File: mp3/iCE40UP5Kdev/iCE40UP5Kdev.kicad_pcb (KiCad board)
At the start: 2 copper layers, 21.8 x 51.9 mm, 57 parts, among them J1 USB4105-GF-A, J2 Left, J3 Right, J4 Conn_02x03_Counter_Clockwise, U1 W25Q32JV, U2 MIC5365-1-2YD5, U3 MIC5318-3-3YD5, U4 ICE40UP5K-SG48ITR, X1 IQXO-791

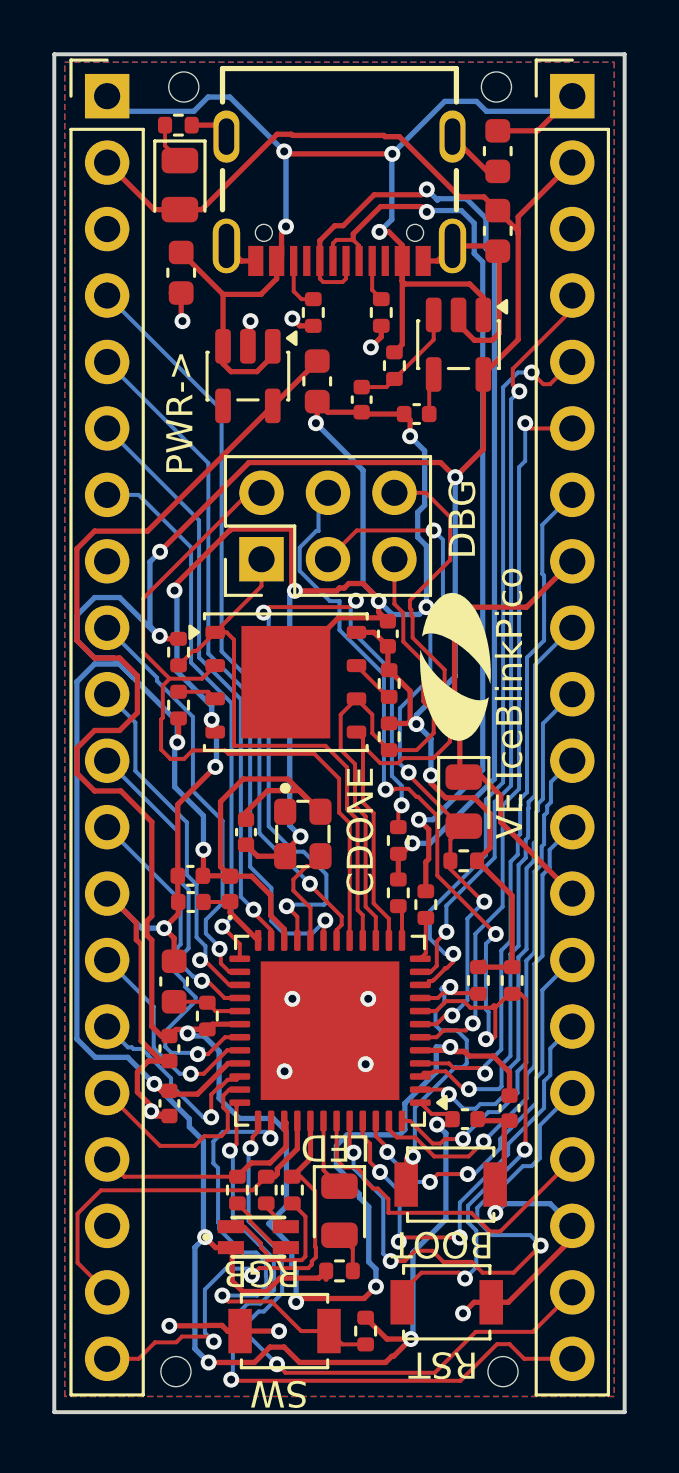
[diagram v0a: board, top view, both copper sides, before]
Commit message: update via spacing
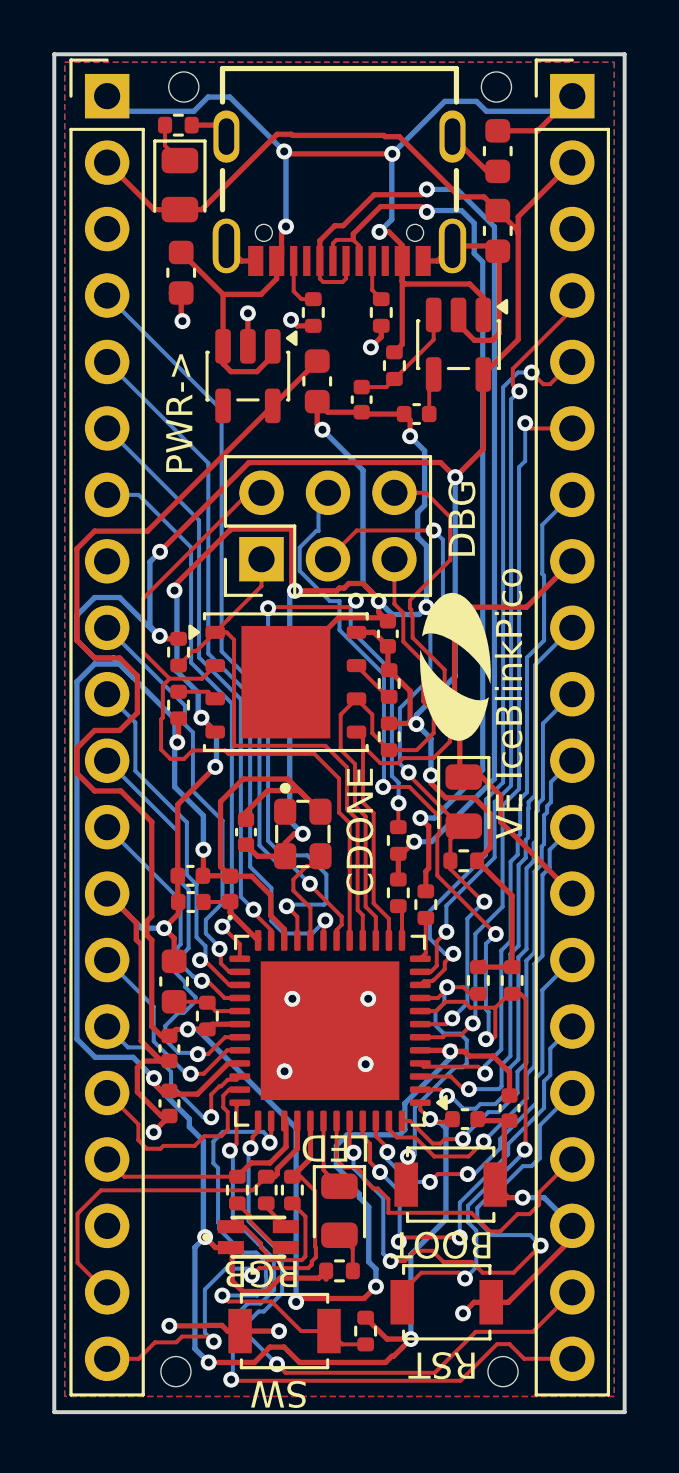
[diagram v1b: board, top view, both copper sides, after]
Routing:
- net +1V2: track 76.0 -> 74.1 mm
- net +3V3: track 178.0 -> 178.8 mm

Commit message: fix gaps in power pour
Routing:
- net +3V3: track 178.8 -> 184.8 mm
